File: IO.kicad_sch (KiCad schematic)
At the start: 6 parts, among them J5 Conn_01x05, J6 Conn_01x05, J7 Conn_01x05, J8 Conn_01x05, Q2 AO3401A

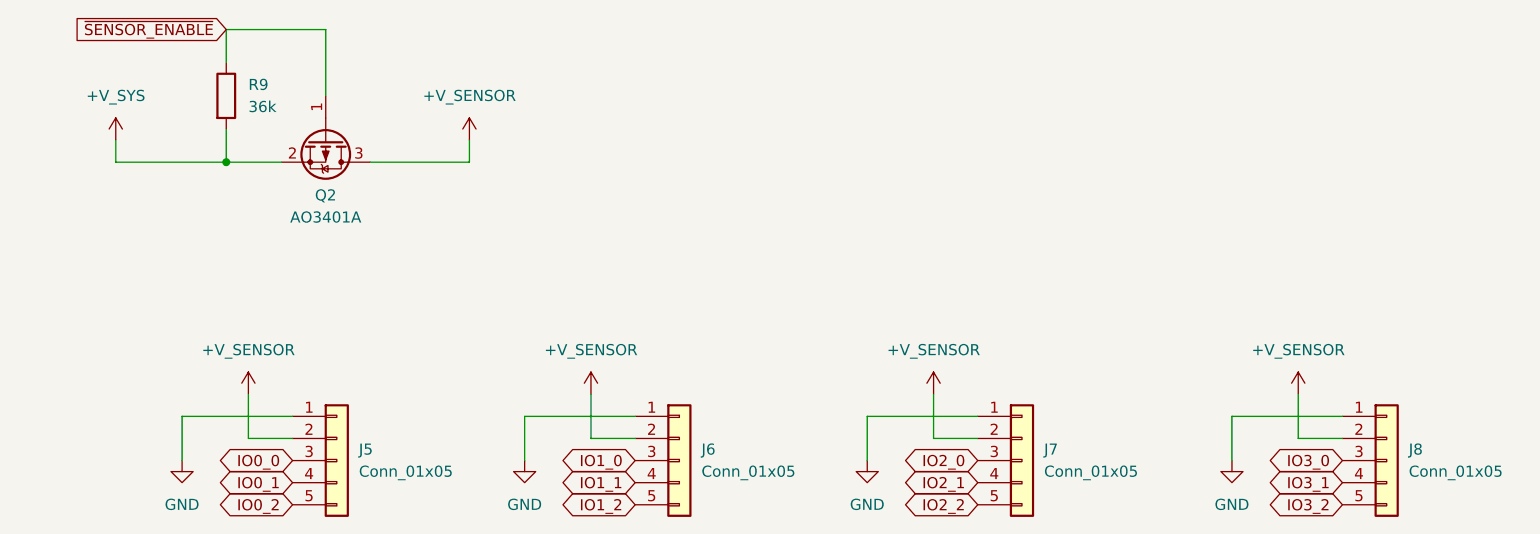
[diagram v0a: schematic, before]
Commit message: completed layout and routing with preliminary matching network
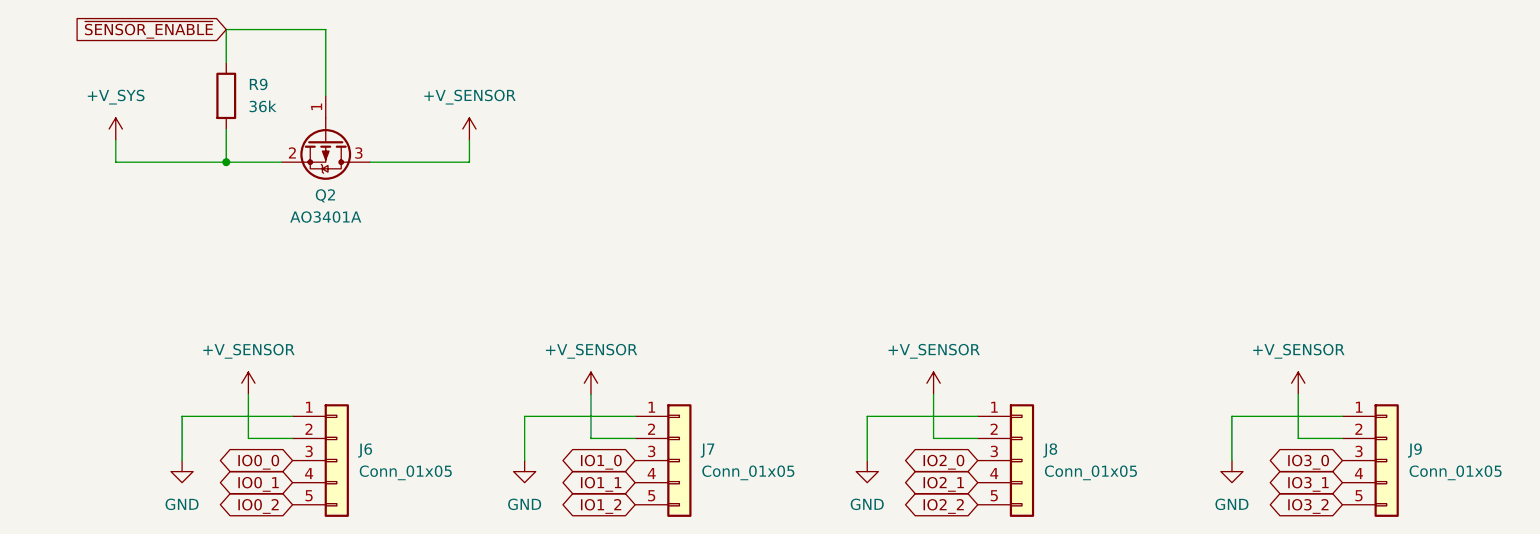
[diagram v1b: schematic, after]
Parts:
- renumbered J5 to J6, J6 to J7, J7 to J8, J8 to J9
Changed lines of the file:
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@@
 		(dnp no)
 		(fields_autoplaced yes)
-		(property "Reference" "#PWR036"
+		(property "Reference" "#PWR040"
 			(at 118.11 99.06 0)
 			(hide yes)
@@
 			(project "WINLAB-LP-Radio-Sensor-Hub"
 				(path "/0de7ee4a-bb98-4bc6-bb89-3afafc4b94b5/7c2f8fd5-667e-47fd-95c9-2d370070e57a"
-					(reference "#PWR036")
+					(reference "#PWR040")
 					(unit 1)
 				)
@@
 		(dnp no)
 		(fields_autoplaced yes)
-		(property "Reference" "#PWR032"
+		(property "Reference" "#PWR038"
 			(at 104.14 69.85 0)
 			(hide yes)
@@
 			(project "WINLAB-LP-Radio-Sensor-Hub"
 				(path "/0de7ee4a-bb98-4bc6-bb89-3afafc4b94b5/7c2f8fd5-667e-47fd-95c9-2d370070e57a"
-					(reference "#PWR032")
+					(reference "#PWR038")
 					(unit 1)
 				)
@@
 		(dnp no)
 		(fields_autoplaced yes)
-		(property "Reference" "#PWR033"
+		(property "Reference" "#PWR037"
 			(at 78.74 99.06 0)
 			(hide yes)
@@
 			(project "WINLAB-LP-Radio-Sensor-Hub"
 				(path "/0de7ee4a-bb98-4bc6-bb89-3afafc4b94b5/7c2f8fd5-667e-47fd-95c9-2d370070e57a"
-					(reference "#PWR033")
+					(reference "#PWR037")
 					(unit 1)
 				)
@@
 		(dnp no)
 		(fields_autoplaced yes)
-		(property "Reference" "#PWR039"
+		(property "Reference" "#PWR043"
 			(at 191.77 109.22 0)
 			(hide yes)
@@
 			(project "WINLAB-LP-Radio-Sensor-Hub"
 				(path "/0de7ee4a-bb98-4bc6-bb89-3afafc4b94b5/7c2f8fd5-667e-47fd-95c9-2d370070e57a"
-					(reference "#PWR039")
+					(reference "#PWR043")
 					(unit 1)
 				)
@@
 		(dnp no)
 		(fields_autoplaced yes)
-		(property "Reference" "J7"
+		(property "Reference" "J8"
 			(at 170.18 101.5999 0)
 			(show_name no)
@@
 			(project "WINLAB-LP-Radio-Sensor-Hub"
 				(path "/0de7ee4a-bb98-4bc6-bb89-3afafc4b94b5/7c2f8fd5-667e-47fd-95c9-2d370070e57a"
-					(reference "J7")
+					(reference "J8")
 					(unit 1)
 				)
@@
 		(dnp no)
 		(fields_autoplaced yes)
-		(property "Reference" "#PWR037"
+		(property "Reference" "#PWR041"
 			(at 149.86 109.22 0)
 			(hide yes)
@@
 			(project "WINLAB-LP-Radio-Sensor-Hub"
 				(path "/0de7ee4a-bb98-4bc6-bb89-3afafc4b94b5/7c2f8fd5-667e-47fd-95c9-2d370070e57a"
-					(reference "#PWR037")
+					(reference "#PWR041")
 					(unit 1)
 				)
@@
 		(dnp no)
 		(fields_autoplaced yes)
-		(property "Reference" "#PWR035"
+		(property "Reference" "#PWR039"
 			(at 110.49 109.22 0)
 			(hide yes)
@@
 			(project "WINLAB-LP-Radio-Sensor-Hub"
 				(path "/0de7ee4a-bb98-4bc6-bb89-3afafc4b94b5/7c2f8fd5-667e-47fd-95c9-2d370070e57a"
-					(reference "#PWR035")
+					(reference "#PWR039")
 					(unit 1)
 				)
@@
 		(dnp no)
 		(fields_autoplaced yes)
-		(property "Reference" "J5"
+		(property "Reference" "J6"
 			(at 91.44 101.5999 0)
 			(show_name no)
@@
 			(project "WINLAB-LP-Radio-Sensor-Hub"
 				(path "/0de7ee4a-bb98-4bc6-bb89-3afafc4b94b5/7c2f8fd5-667e-47fd-95c9-2d370070e57a"
-					(reference "J5")
+					(reference "J6")
 					(unit 1)
 				)
@@
 		(dnp no)
 		(fields_autoplaced yes)
-		(property "Reference" "#PWR034"
+		(property "Reference" "#PWR036"
 			(at 71.12 109.22 0)
 			(hide yes)
@@
 			(project "WINLAB-LP-Radio-Sensor-Hub"
 				(path "/0de7ee4a-bb98-4bc6-bb89-3afafc4b94b5/7c2f8fd5-667e-47fd-95c9-2d370070e57a"
-					(reference "#PWR034")
+					(reference "#PWR036")
 					(unit 1)
 				)
@@
 		(dnp no)
 		(fields_autoplaced yes)
-		(property "Reference" "#PWR038"
+		(property "Reference" "#PWR042"
 			(at 157.48 99.06 0)
 			(hide yes)
@@
 			(project "WINLAB-LP-Radio-Sensor-Hub"
 				(path "/0de7ee4a-bb98-4bc6-bb89-3afafc4b94b5/7c2f8fd5-667e-47fd-95c9-2d370070e57a"
-					(reference "#PWR038")
+					(reference "#PWR042")
 					(unit 1)
 				)
@@
 		(dnp no)
 		(fields_autoplaced yes)
-		(property "Reference" "#PWR031"
+		(property "Reference" "#PWR035"
 			(at 63.5 69.85 0)
 			(hide yes)
@@
 			(project "WINLAB-LP-Radio-Sensor-Hub"
 				(path "/0de7ee4a-bb98-4bc6-bb89-3afafc4b94b5/7c2f8fd5-667e-47fd-95c9-2d370070e57a"
-					(reference "#PWR031")
+					(reference "#PWR035")
 					(unit 1)
 				)
@@
 		(dnp no)
 		(fields_autoplaced yes)
-		(property "Reference" "J6"
+		(property "Reference" "J7"
 			(at 130.81 101.5999 0)
 			(show_name no)
@@
 			(project "WINLAB-LP-Radio-Sensor-Hub"
 				(path "/0de7ee4a-bb98-4bc6-bb89-3afafc4b94b5/7c2f8fd5-667e-47fd-95c9-2d370070e57a"
-					(reference "J6")
+					(reference "J7")
 					(unit 1)
 				)
@@
 		(dnp no)
 		(fields_autoplaced yes)
-		(property "Reference" "J8"
+		(property "Reference" "J9"
 			(at 212.09 101.5999 0)
 			(show_name no)
@@
 			(project "WINLAB-LP-Radio-Sensor-Hub"
 				(path "/0de7ee4a-bb98-4bc6-bb89-3afafc4b94b5/7c2f8fd5-667e-47fd-95c9-2d370070e57a"
-					(reference "J8")
+					(reference "J9")
 					(unit 1)
 				)
@@
 		(dnp no)
 		(fields_autoplaced yes)
-		(property "Reference" "#PWR040"
+		(property "Reference" "#PWR044"
 			(at 199.39 99.06 0)
 			(hide yes)
@@
 			(project "WINLAB-LP-Radio-Sensor-Hub"
 				(path "/0de7ee4a-bb98-4bc6-bb89-3afafc4b94b5/7c2f8fd5-667e-47fd-95c9-2d370070e57a"
-					(reference "#PWR040")
-					(unit 1)
-				)
+					(reference "#PWR044")
+					(unit 1)
+				)

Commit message: add LCSC part number properties in preparation for JLCPCB assembly order
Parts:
- Q2: LCSC Part Number (none) -> C15127
- R9: LCSC Part Number (none) -> C23153
